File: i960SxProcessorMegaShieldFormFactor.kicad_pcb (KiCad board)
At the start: 4 copper layers, 101.6 x 53.3 mm, 44 parts, among them P1 Power, P2 Data Lines Lower, P3 Data Lines Upper, P4 Address Lines, P5 PWM, P6 Serializable Pins, P7 1284p Direct Connection, U1 74HC245, U2 74HC245, U3 80960Sx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

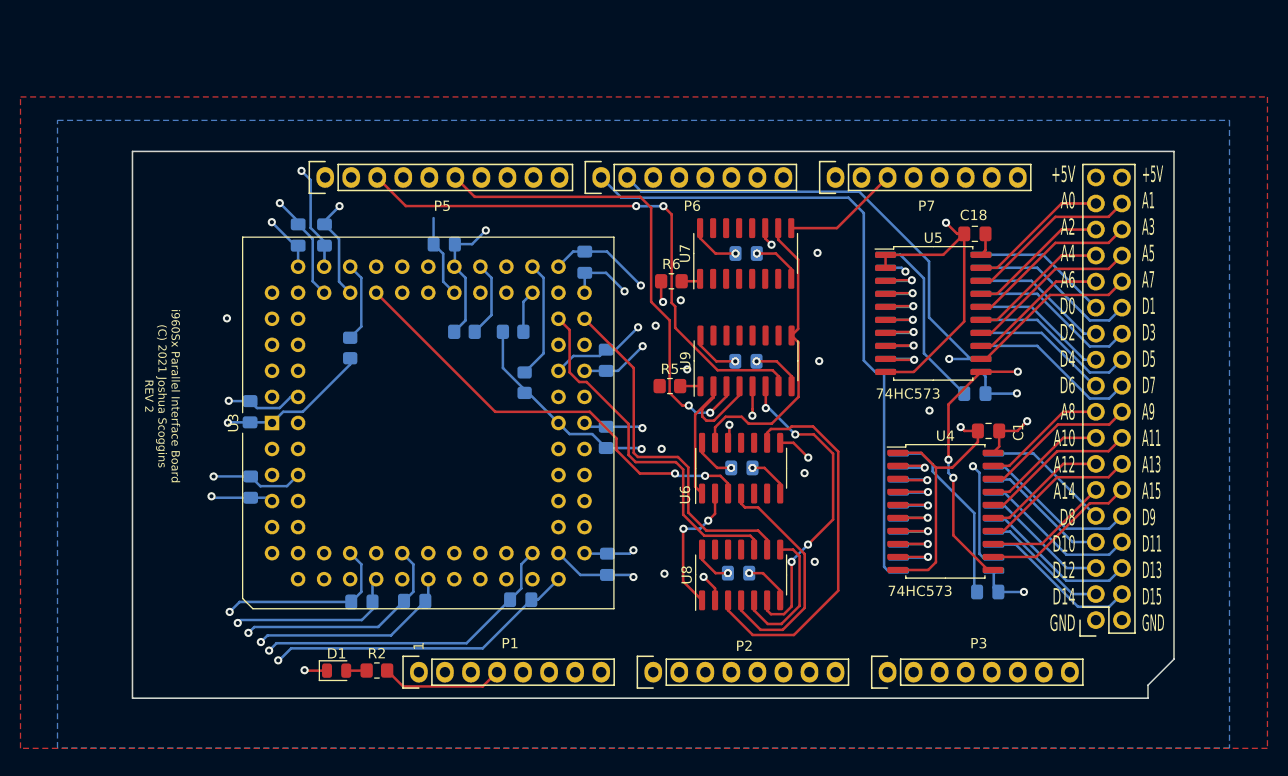
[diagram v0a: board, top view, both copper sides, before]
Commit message: Put the data and address lines back into the previous design
Maximizes compatibility?
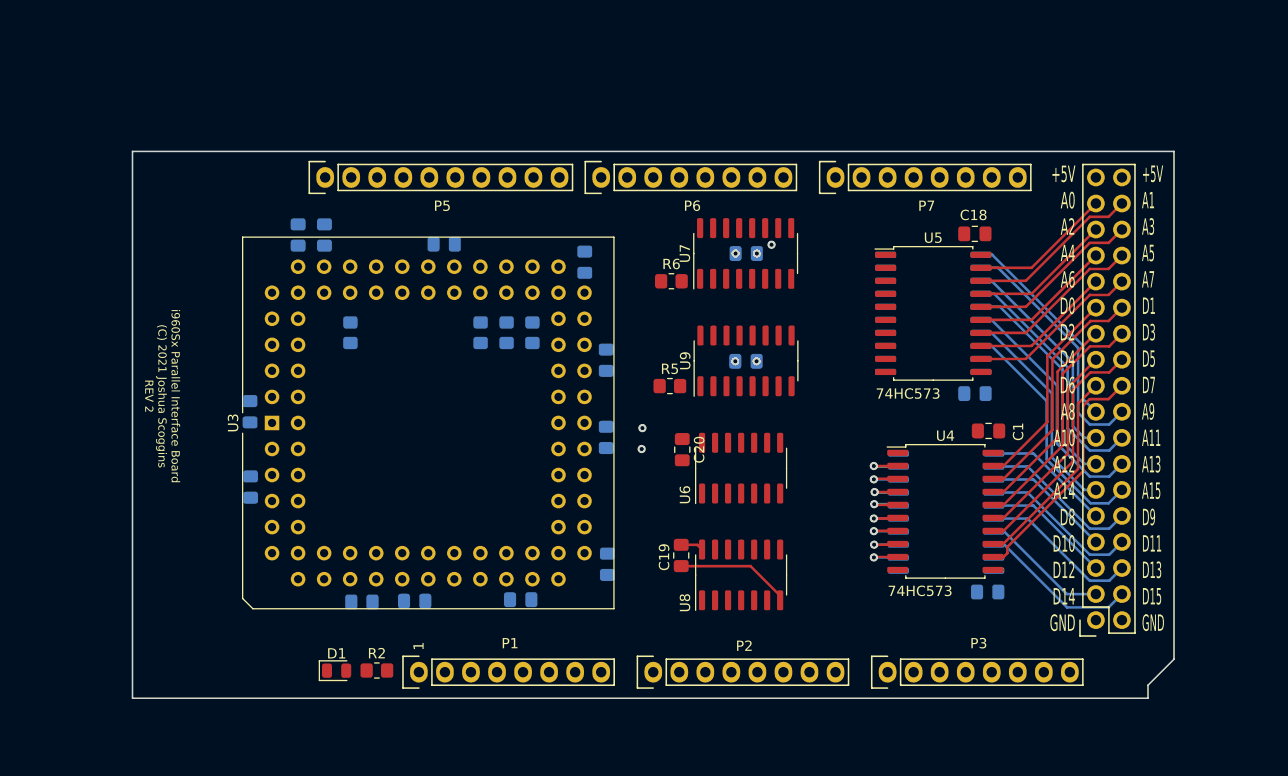
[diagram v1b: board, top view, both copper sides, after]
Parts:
- C19, C20: moved to F.Cu
- moved C20 6.08 mm to (157.0, 97.4), turned to 270 degrees
- moved C19 5.85 mm to (156.9, 107.7), turned to 270 degrees
- moved R7 4.93 mm to (142.4, 86.0)
- moved R3 1.58 mm to (137.3, 86.0), turned to 90 degrees
- moved R1 1.49 mm to (124.6, 86.0)
- moved R4 0.64 mm to (139.9, 86.0), turned to 90 degrees
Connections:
- P4 pad 11: /A14 -> /D6
- P4 pad 12: /A15 -> /D7
- P4 pad 13: /A12 -> /D4
- P4 pad 14: /A13 -> /D5
- P4 pad 15: /A10 -> /D2
- P4 pad 16: /A11 -> /D3
- P4 pad 17: /A8 -> /D0_OUT
- P4 pad 18: /A9 -> /D1
- P4 pad 19: /D6 -> /A14
- P4 pad 20: /D7 -> /A15
- P4 pad 21: /D4 -> /A12
- P4 pad 22: /D5 -> /A13
- P4 pad 23: /D2 -> /A10
- P4 pad 24: /D3 -> /A11
- P4 pad 25: /D0_OUT -> /A8
- P4 pad 26: /D1 -> /A9
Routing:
- net GND: track 296.4 -> 11.3 mm, vias 23 -> 3
- net +5V: track 251.0 -> 2.22 mm, vias 26 -> 3
- net /ALE: track 121.6 -> 0.00 mm, vias 3 -> 0
- net /~DEN: track 99.9 -> 0.00 mm, vias 2 -> 0
- net /DT\~R: track 90.2 -> 0.00 mm
- net /~BE1: track 77.4 -> 0.00 mm
- net /~BE0: track 77.1 -> 0.00 mm
- net /A17: track 76.0 -> 0.00 mm
- net /A29: track 75.1 -> 0.00 mm
- net /A22: track 74.2 -> 0.00 mm
- net /A16: track 74.0 -> 0.00 mm
- net /A19: track 73.4 -> 0.00 mm
- net /A26: track 72.5 -> 0.00 mm
- net /A28: track 72.2 -> 0.00 mm
- net /A18: track 71.4 -> 0.00 mm
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- removed copper zone on F.Cu, net +5V
- removed copper zone on B.Cu, net GND

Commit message: Fix labeling
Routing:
- net /AD4: track 0.00 -> 5.29 mm, vias 0 -> 1
- net /AD1: track 0.00 -> 5.25 mm, vias 0 -> 1
- net /AD2: track 0.00 -> 5.22 mm, vias 0 -> 1
- net /AD5: track 0.00 -> 5.21 mm, vias 0 -> 1
- net /AD3: track 0.00 -> 5.20 mm, vias 0 -> 1
- net /AD7: track 0.00 -> 5.20 mm, vias 0 -> 1
- net /AD6: track 0.00 -> 5.16 mm, vias 0 -> 1
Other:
- board text added: "+5V A0 A2 A4 A6 A8 A10 A12 A14 D0 D2 D4 D6 D8 D10 D12 D14 GND"
- board text added: "+5V A1 A3 A5 A7 A9 A11 A13 A15 D1 D3 D5 D7 D9 D11 D13 D15 GND"
- board text removed: "+5V A0 A2 A4 A6 D0 D2 D4 D6 A8 A10 A12 A14 D8 D10 D12 D14 GND"
- board text removed: "+5V A1 A3 A5 A7 D1 D3 D5 D7 A9 A11 A13 A15 D9 D11 D13 D15 GND"
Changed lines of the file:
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@@
     (thickness 1.6)
     (drawings 10)
-    (tracks 195)
+    (tracks 229)
     (zones 0)
     (modules 44)
@@
     )
   )
-  (gr_text "+5V\nA1\nA3\nA5\nA7\nD1\nD3\nD5\nD7\nA9\nA11\nA13\nA15\nD9\nD11\nD13\nD15\nGND" (at 201.85126 92.456) (layer F.SilkS)
-    (effects (font (size 1.6 0.7) (thickness 0.1)) (justify left))
-  )
-  (gr_text "+5V\nA0\nA2\nA4\nA6\nD0\nD2\nD4\nD6\nA8\nA10\nA12\nA14\nD8\nD10\nD12\nD14\nGND" (at 195.36664 92.46108) (layer F.SilkS)
-    (effects (font (size 1.6 0.8) (thickness 0.1)) (justify right))
+  (gr_text "+5V\nA1\nA3\nA5\nA7\nA9\nA11\nA13\nA15\nD1\nD3\nD5\nD7\nD9\nD11\nD13\nD15\nGND" (at 201.85126 92.456) (layer F.SilkS)
+    (effects (font (size 1.6 0.7) (thickness 0.15)) (justify left))
+  )
+  (gr_text "+5V\nA0\nA2\nA4\nA6\nA8\nA10\nA12\nA14\nD0\nD2\nD4\nD6\nD8\nD10\nD12\nD14\nGND" (at 195.36664 92.46108) (layer F.SilkS)
+    (effects (font (size 1.6 0.8) (thickness 0.15)) (justify right))
   )
   (gr_text "i960Sx Parallel Interface Board\n(C) 2021 Joshua Scoggins\nREV 2" (at 106.2736 92.19946 -90) (layer F.SilkS)
@@
   (segment (start 198.596601 112.807399) (end 199.898 111.506) (width 0.25) (layer Back) (net 41))
   (segment (start 187.39538 106.68254) (end 188.42038 106.68254) (width 0.25) (layer Back) (net 41))
+  (via (at 174.2567 82.26552) (size 0.8) (drill 0.4) (layers Front Back) (net 81) (status 40000))
+  (segment (start 174.30242 82.2198) (end 174.2567 82.26552) (width 0.25) (layer Front) (net 81))
+  (segment (start 176.84062 82.2198) (end 174.30242 82.2198) (width 0.25) (layer Front) (net 81))
+  (segment (start 176.80252 82.26552) (end 176.85078 82.21726) (width 0.25) (layer Back) (net 81))
+  (segment (start 174.2567 82.26552) (end 176.80252 82.26552) (width 0.25) (layer Back) (net 81))
+  (via (at 174.23892 84.84616) (size 0.8) (drill 0.4) (layers Front Back) (net 82) (status 40000))
+  (segment (start 174.32528 84.7598) (end 174.23892 84.84616) (width 0.25) (layer Front) (net 82))
+  (segment (start 176.84062 84.7598) (end 174.32528 84.7598) (width 0.25) (layer Front) (net 82))
+  (segment (start 176.76188 84.84616) (end 176.85078 84.75726) (width 0.25) (layer Back) (net 82))
+  (segment (start 174.23892 84.84616) (end 176.76188 84.84616) (width 0.25) (layer Back) (net 82))
+  (via (at 174.26432 87.2998) (size 0.8) (drill 0.4) (layers Front Back) (net 83) (status 40000))
+  (segment (start 176.84062 87.2998) (end 174.26432 87.2998) (width 0.25) (layer Front) (net 83))
+  (segment (start 176.84824 87.2998) (end 176.85078 87.29726) (width 0.25) (layer Back) (net 83))
+  (segment (start 174.26432 87.2998) (end 176.84824 87.2998) (width 0.25) (layer Back) (net 83))
+  (via (at 174.2313 80.92186) (size 0.8) (drill 0.4) (layers Front Back) (net 86) (status 40000))
+  (segment (start 174.2567 80.94726) (end 174.2313 80.92186) (width 0.25) (layer Back) (net 86))
+  (segment (start 176.85078 80.94726) (end 174.2567 80.94726) (width 0.25) (layer Back) (net 86))
+  (segment (start 176.81268 80.92186) (end 176.84062 80.9498) (width 0.25) (layer Front) (net 86))
+  (segment (start 174.2313 80.92186) (end 176.81268 80.92186) (width 0.25) (layer Front) (net 86))
+  (via (at 174.24908 83.49488) (size 0.8) (drill 0.4) (layers Front Back) (net 87) (status 40000))
+  (segment (start 174.2567 83.48726) (end 174.24908 83.49488) (width 0.25) (layer Back) (net 87))
+  (segment (start 176.85078 83.48726) (end 174.2567 83.48726) (width 0.25) (layer Back) (net 87))
+  (segment (start 176.83554 83.49488) (end 176.84062 83.4898) (width 0.25) (layer Front) (net 87))
+  (segment (start 174.24908 83.49488) (end 176.83554 83.49488) (width 0.25) (layer Front) (net 87))
+  (segment (start 174.26686 86.02726) (end 174.24908 86.04504) (width 0.25) (layer Back) (net 88))
+  (via (at 174.24908 86.04504) (size 0.8) (drill 0.4) (layers Front Back) (net 88) (status 40000))
+  (segment (start 176.85078 86.02726) (end 174.26686 86.02726) (width 0.25) (layer Back) (net 88))
+  (segment (start 176.82538 86.04504) (end 176.84062 86.0298) (width 0.25) (layer Front) (net 88))
+  (segment (start 174.24908 86.04504) (end 176.82538 86.04504) (width 0.25) (layer Front) (net 88))
+  (segment (start 174.27956 88.56726) (end 174.2567 88.5444) (width 0.25) (layer Back) (net 89))
+  (via (at 174.2567 88.5444) (size 0.8) (drill 0.4) (layers Front Back) (net 89) (status 40000))
+  (segment (start 176.85078 88.56726) (end 174.27956 88.56726) (width 0.25) (layer Back) (net 89))
+  (segment (start 176.81522 88.5444) (end 176.84062 88.5698) (width 0.25) (layer Front) (net 89))
+  (segment (start 174.2567 88.5444) (end 176.81522 88.5444) (width 0.25) (layer Front) (net 89))
   (via (at 175.69434 100.31476) (size 0.8) (drill 0.4) (layers Front Back) (net 90) (status 40000))
   (segment (start 175.74514 100.26396) (end 175.69434 100.31476) (width 0.25) (layer Front) (net 90))

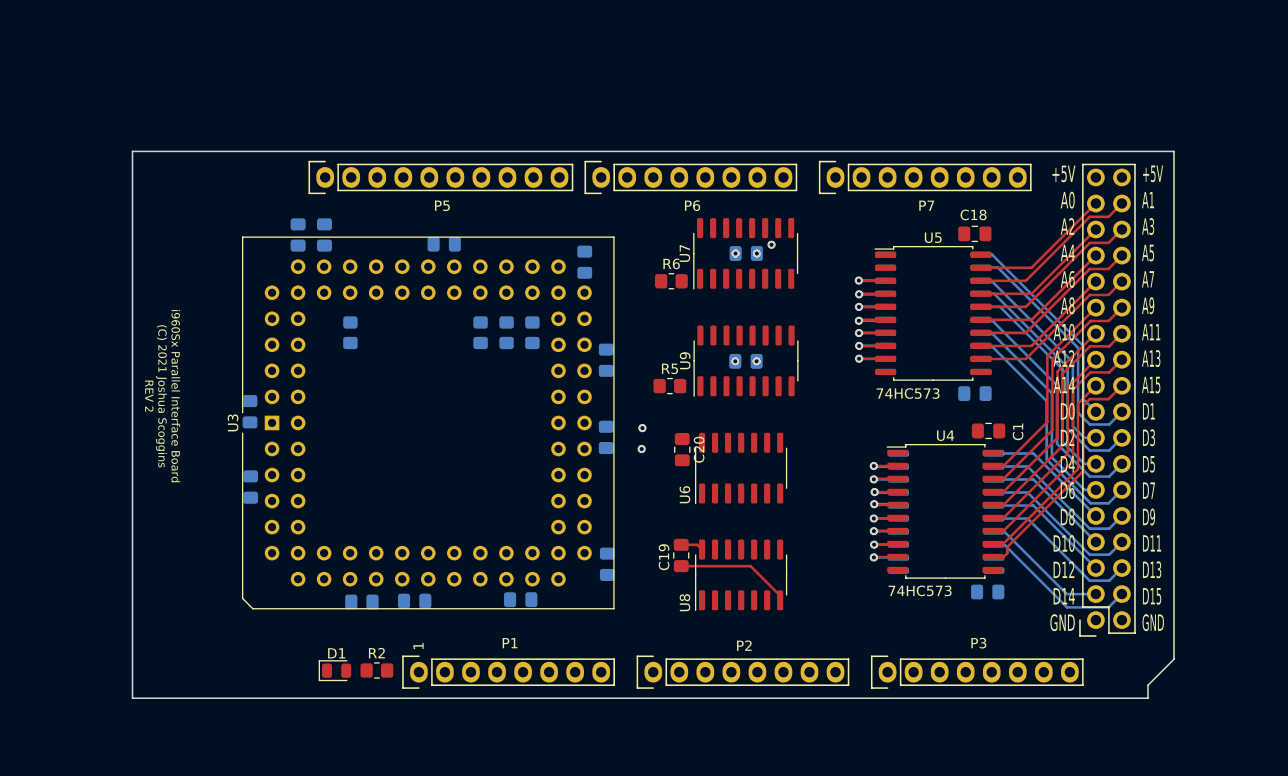
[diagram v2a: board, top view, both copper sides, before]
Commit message: Rearrange aux hardware to reduce via count
Start routing the rest of the traces out of the i960
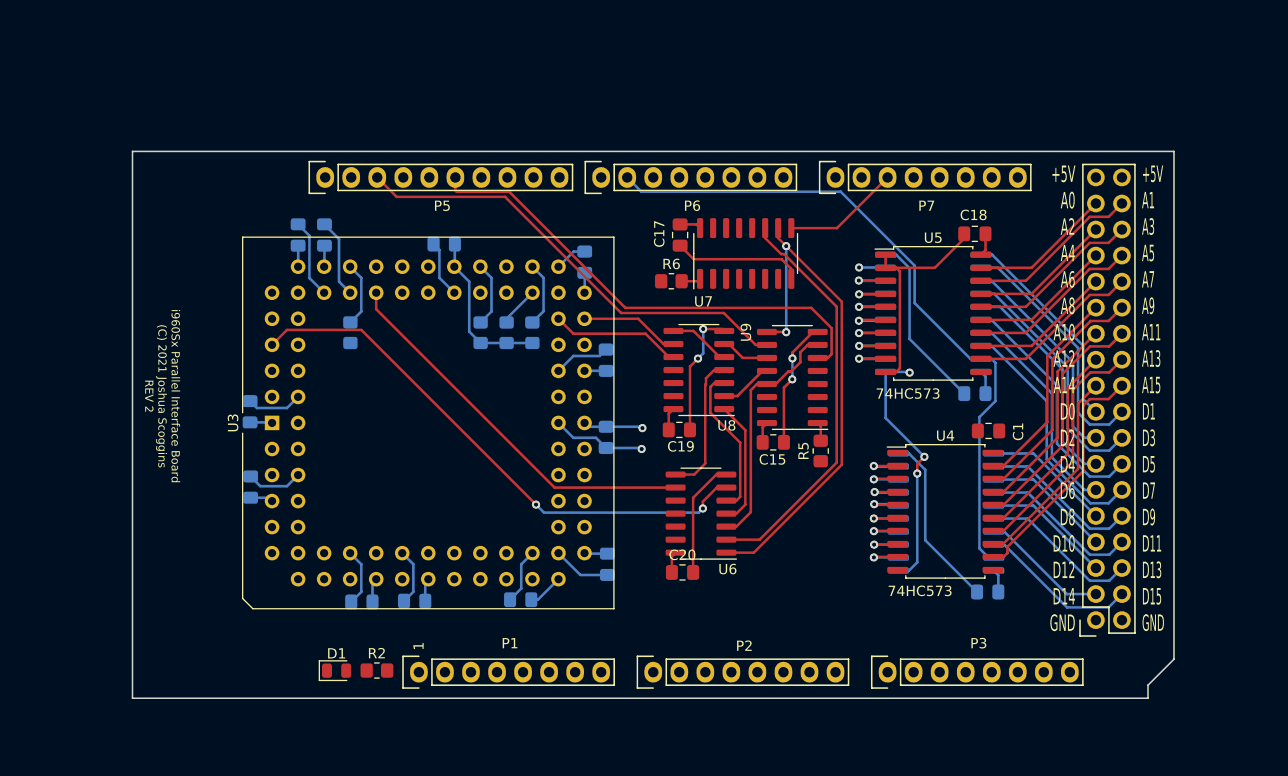
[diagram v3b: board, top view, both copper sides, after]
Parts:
- C15, C17: moved to F.Cu
- moved U8 20.4 mm to (158.6, 89.7), turned to 180 degrees
- moved R5 16.0 mm to (170.5, 97.5), turned to 90 degrees
- moved C19 12.3 mm to (156.7, 95.5), turned to 0 degrees
- moved C20 12.0 mm to (157.0, 109.4), turned to 0 degrees
- moved C15 8.35 mm to (165.9, 96.7)
- moved C17 6.69 mm to (156.8, 76.5), turned to 270 degrees
- moved U6 5.91 mm to (158.8, 103.7), turned to 180 degrees
- moved U9 4.80 mm to (167.7, 90.4), turned to 180 degrees
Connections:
- U6 pad 1: /Sheet62305775/Z0 -> /Sheet62305775/CLKSRC0
- U6 pad 12: Net-(U6-Pad12) -> (no net)
- U6 pad 13: /Sheet62305775/CLKSRC0 -> (no net)
- U6 pad 3: /~BLAST~\~FAIL~ -> /Sheet62305775/Z0
- U6 pad 5: (no net) -> Net-(U6-Pad5)
- U6 pad 6: (no net) -> /~READY960
- U6 pad 8: /~READY960 -> Net-(U6-Pad8)
- U6 pad 9: Net-(U6-Pad9) -> /~BLAST~\~FAIL~
- U7 pad 11: Net-(U6-Pad12) -> Net-(U6-Pad2)
- U8 pad 1: Net-(U6-Pad2) -> Net-(U6-Pad4)
- U8 pad 3: Net-(U6-Pad9) -> Net-(U6-Pad5)
- U8 pad 4: Net-(U6-Pad4) -> Net-(U6-Pad8)
- U9 pad 10: Net-(U9-Pad10) -> /MCU_FAIL
- U9 pad 11: Net-(U9-Pad11) -> /Sheet62305775/FAIL_SYNC
- U9 pad 12: Net-(U9-Pad12) -> /Sheet62305775/Z1
- U9 pad 13: Net-(U9-Pad13) -> /Sheet62305775/Z0
- U9 pad 2: /Sheet62305775/Z0 -> Net-(U9-Pad2)
- U9 pad 3: /~READY -> Net-(U9-Pad3)
- U9 pad 4: /Sheet62305775/Z0 -> Net-(U9-Pad4)
- U9 pad 5: /Sheet62305775/Z1 -> Net-(U9-Pad5)
- U9 pad 6: /Sheet62305775/FAIL_SYNC -> /~READY
- U9 pad 7: /MCU_FAIL -> /Sheet62305775/Z0
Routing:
- net GND: track 11.3 -> 152.5 mm, vias 3 -> 5
- net /~DEN: track 0.00 -> 96.7 mm
- net /DT\~R: track 0.00 -> 93.2 mm, vias 0 -> 3
- net +5V: track 2.22 -> 86.2 mm, vias 3 -> 1
- net /A17: track 0.00 -> 79.6 mm
- net /A16: track 0.00 -> 77.6 mm
- net /A19: track 0.00 -> 77.1 mm
- net /A18: track 0.00 -> 75.1 mm
- net /A21: track 0.00 -> 74.5 mm
- net /A20: track 0.00 -> 72.5 mm
- net /A29: track 0.00 -> 72.5 mm
- net /A31: track 0.00 -> 71.8 mm
- net /A26: track 0.00 -> 70.2 mm
- net /A28: track 0.00 -> 69.6 mm
- net /A30: track 0.00 -> 68.9 mm
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
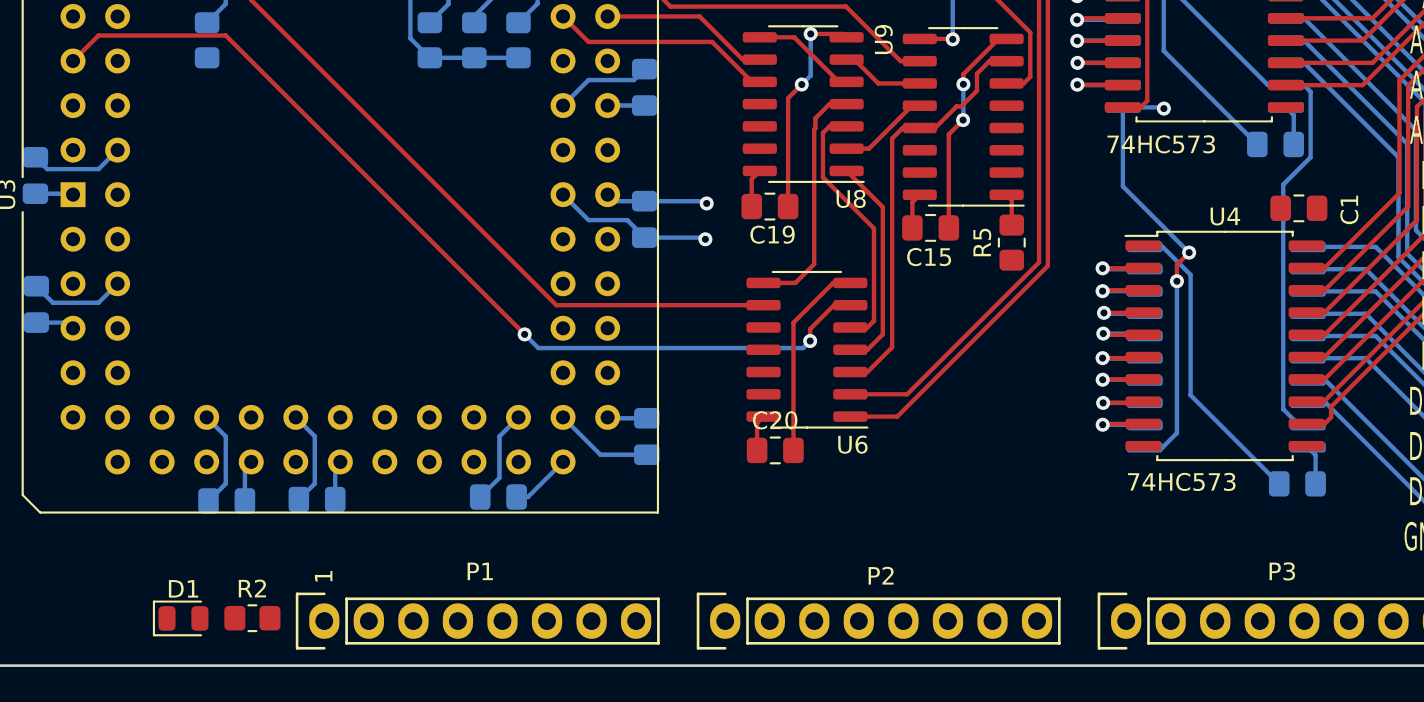
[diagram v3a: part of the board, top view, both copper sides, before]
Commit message: Finished non power routing
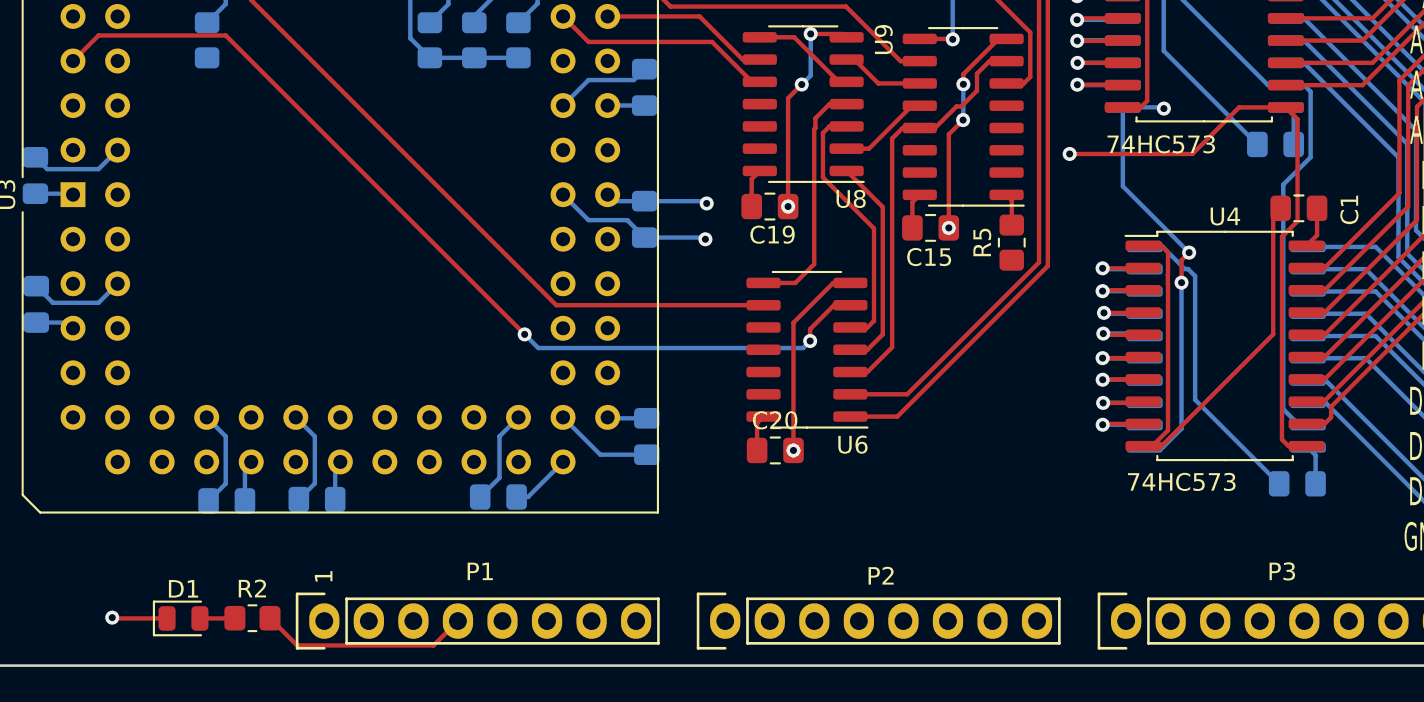
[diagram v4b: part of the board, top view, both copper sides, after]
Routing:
- net /ALE: track 27.3 -> 120.1 mm, vias 0 -> 1
- net /CLKO: track 11.4 -> 51.5 mm
- net /~INT0: track 3.94 -> 41.7 mm
- net /~RESET960: track 6.34 -> 42.1 mm
- net GND: track 152.5 -> 186.6 mm, vias 5 -> 9
- net /INT2: track 0.00 -> 32.5 mm
- net /INT1: track 0.00 -> 30.7 mm
- net /~INT3: track 6.33 -> 34.4 mm
- net +3V3: track 0.00 -> 11.9 mm
- net /DT\~R: track 93.2 -> 100.7 mm
- net +5V: track 86.2 -> 88.5 mm
- net Net-(D1-Pad2): track 0.00 -> 2.00 mm
- net /W\~R~: track 28.9 -> 28.1 mm
- net /~DEN: track 96.7 -> 96.0 mm

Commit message: Power routing done?
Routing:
- net +5V: track 88.5 -> 212.3 mm, vias 1 -> 19
- net GND: track 186.6 -> 291.8 mm, vias 9 -> 25
- net /A21: track 74.5 -> 70.9 mm
- net /A19: track 77.1 -> 73.4 mm
- net /A20: track 72.5 -> 68.9 mm
- net /A18: track 75.1 -> 71.4 mm
- net /A17: track 79.6 -> 76.0 mm
- net /A16: track 77.6 -> 74.0 mm
- net /Sheet62305775/CLKSRC0: track 50.7 -> 52.9 mm
- net Net-(U6-Pad2): track 39.8 -> 42.0 mm
- net /~DEN: track 96.0 -> 97.7 mm
- added copper zone on In2.Cu, net +5V
- added copper zone on B.Cu, net GND
